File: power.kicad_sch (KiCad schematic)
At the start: 29 parts, among them J3 Conn_01x03_Male, Q1 DMP1045U-7, Q2 UMW8205A, U1 TD5830B, U2 TP4056M, U3 DW01A-G

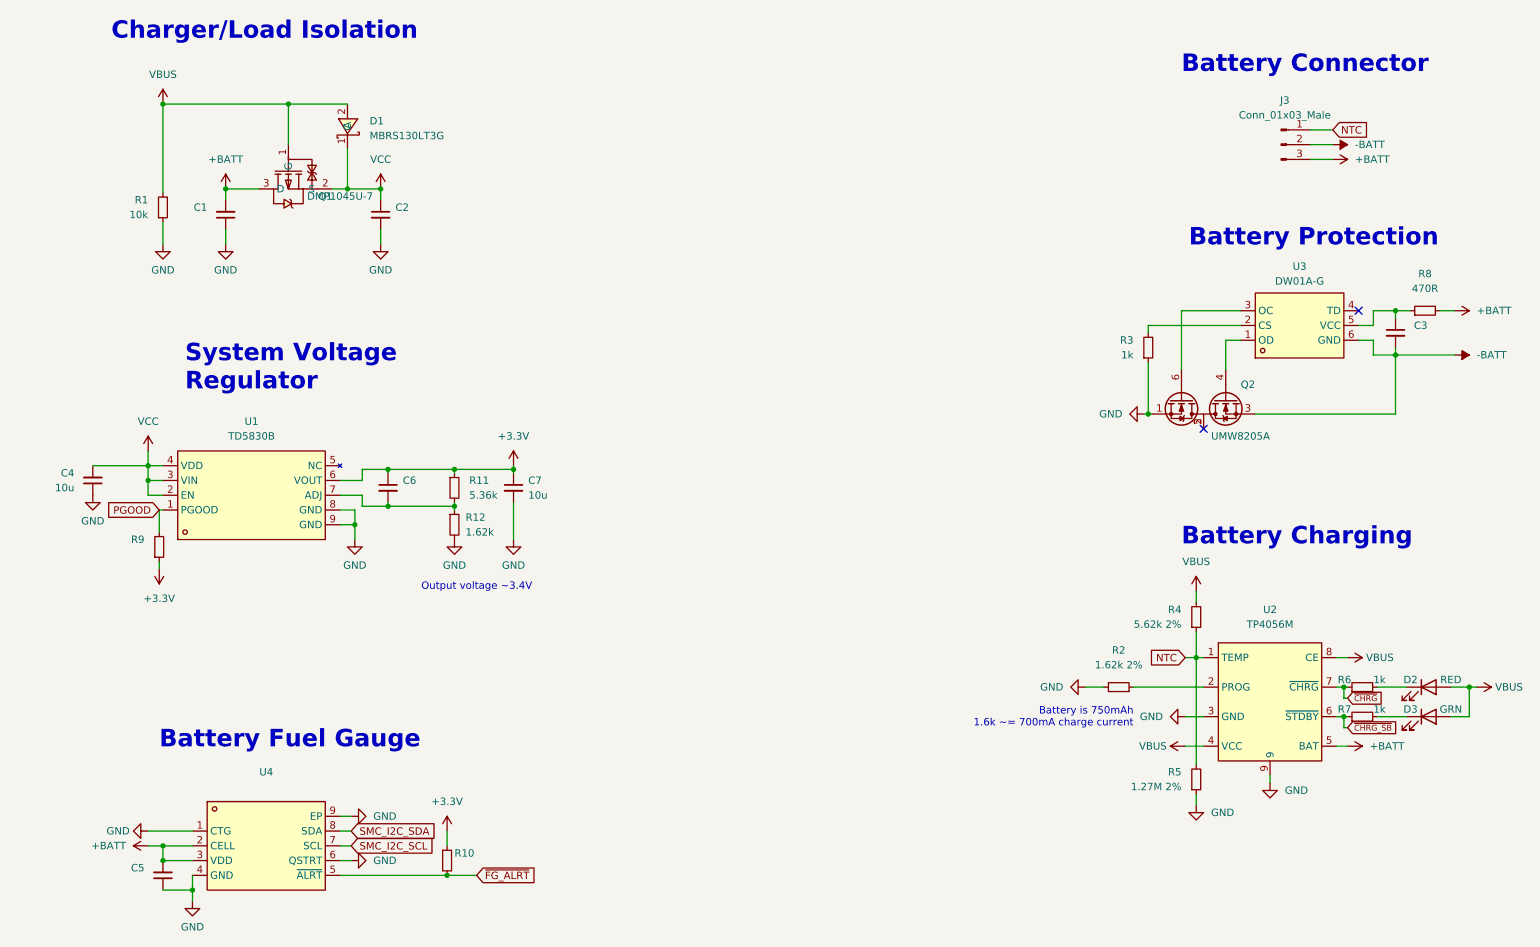
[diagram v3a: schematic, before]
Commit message: analysis: specify pi will be powered directly from VCC
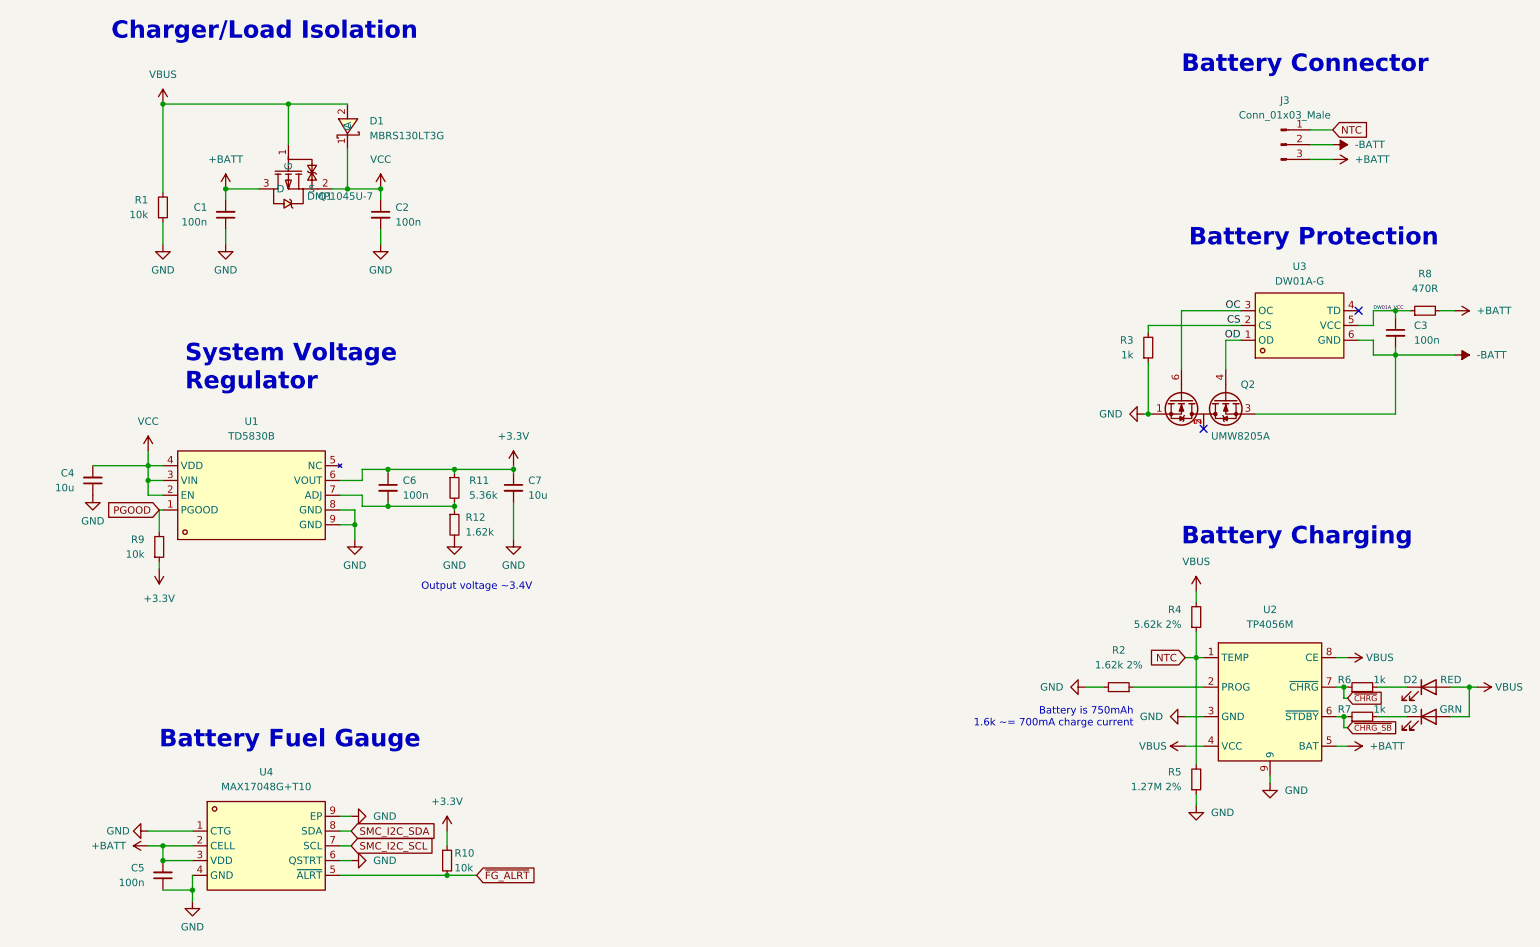
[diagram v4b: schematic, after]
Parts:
- C1, C2, C3, C5, C6: value (none) -> 100n; footprint (none) -> Capacitor_SMD:C_0402_1005Metric
- C4, C7: footprint (none) -> Capacitor_SMD:C_0402_1005Metric
- D2, D3: footprint (none) -> LED_SMD:LED_0201_0603Metric
- R1, R11, R12, R2, R3, R4, R5, R6, R7, R8: footprint (none) -> Resistor_SMD:R_0402_1005Metric
- R10, R9: value (none) -> 10k; footprint (none) -> Resistor_SMD:R_0402_1005Metric
- U4: value (none) -> MAX17048G+T10
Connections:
- net OD: now reaches Q2.4 (G2), U3.1 (OD)
- net CS: now reaches R3.2, U3.2 (CS)
- net OC: now reaches Q2.6 (G1), U3.3 (OC)
- net DW01A_VCC: now reaches C3.1, R8.1, U3.5 (VCC)
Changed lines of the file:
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@@
     (effects (font (size 3 3) (thickness 0.6) bold) (justify left bottom))
+  )
+  (label "DW01A_VCC" (at 253.365 67.945 0)
+    (effects (font (size 0.6 0.6)) (justify left bottom))
+  )
+  (label "OC" (at 230.505 67.945 180)
+    (effects (font (size 1.27 1.27)) (justify right bottom))
+  )
+  (label "CS" (at 230.505 70.485 180)
+    (effects (font (size 1.27 1.27)) (justify right bottom))
+  )
+  (label "OD" (at 230.505 73.025 180)
+    (effects (font (size 1.27 1.27)) (justify right bottom))
   )
   (global_label "PGOOD" (shape input) (at 44.45 102.235 180) (fields_autoplaced)
@@
       (effects (font (size 1.27 1.27)) (justify right))
     )
-    (property "Footprint" "" (id 2) (at 45.085 50.165 0)
+    (property "Footprint" "Resistor_SMD:R_0402_1005Metric" (id 2) (at 45.085 50.165 0)
       (effects (font (size 1.27 1.27)) hide)
     )
@@
       (effects (font (size 1.27 1.27)) (justify right))
     )
-    (property "Footprint" "" (id 2) (at 33.02 97.155 0)
+    (property "Footprint" "Capacitor_SMD:C_0402_1005Metric" (id 2) (at 33.02 97.155 0)
       (effects (font (size 1.27 1.27)) hide)
     )
@@
       (effects (font (size 1.27 1.27)) (justify right))
     )
-    (property "Footprint" "" (id 2) (at 222.885 120.65 0)
+    (property "Footprint" "Resistor_SMD:R_0402_1005Metric" (id 2) (at 222.885 120.65 0)
       (effects (font (size 1.27 1.27)) hide)
     )
@@
     )
     (property "Value" "RED" (id 1) (at 266.7 131.445 0))
-    (property "Footprint" "" (id 2) (at 262.89 132.715 0)
+    (property "Footprint" "LED_SMD:LED_0201_0603Metric" (id 2) (at 262.89 132.715 0)
       (effects (font (size 1.27 1.27)) hide)
     )
@@
       (effects (font (size 1.27 1.27)) (justify right))
     )
-    (property "Footprint" "" (id 2) (at 251.46 132.715 0)
+    (property "Footprint" "Resistor_SMD:R_0402_1005Metric" (id 2) (at 251.46 132.715 0)
       (effects (font (size 1.27 1.27)) hide)
     )
@@
     )
     (property "Value" "GRN" (id 1) (at 266.7 136.525 0))
-    (property "Footprint" "" (id 2) (at 262.89 137.795 0)
+    (property "Footprint" "LED_SMD:LED_0201_0603Metric" (id 2) (at 262.89 137.795 0)
       (effects (font (size 1.27 1.27)) hide)
     )
@@
       (effects (font (size 1.27 1.27)) (justify left))
     )
-    (property "Footprint" "" (id 2) (at 105.41 98.425 0)
+    (property "Footprint" "Capacitor_SMD:C_0402_1005Metric" (id 2) (at 105.41 98.425 0)
       (effects (font (size 1.27 1.27)) hide)
     )
@@
     (property "Reference" "R2" (id 0) (at 209.55 126.365 90))
     (property "Value" "1.62k 2%" (id 1) (at 209.55 128.905 90))
-    (property "Footprint" "" (id 2) (at 209.55 132.715 0)
+    (property "Footprint" "Resistor_SMD:R_0402_1005Metric" (id 2) (at 209.55 132.715 0)
       (effects (font (size 1.27 1.27)) hide)
     )
@@
       (effects (font (size 1.27 1.27)) (justify right))
     )
-    (property "Footprint" "" (id 2) (at 251.46 137.795 0)
+    (property "Footprint" "Resistor_SMD:R_0402_1005Metric" (id 2) (at 251.46 137.795 0)
       (effects (font (size 1.27 1.27)) hide)
     )
@@
       (effects (font (size 1.27 1.27)) (justify left))
     )
-    (property "Value" "" (id 1) (at 260.35 73.0312 0)
-      (effects (font (size 1.27 1.27)) (justify left))
-    )
-    (property "Footprint" "" (id 2) (at 257.175 71.755 0)
+    (property "Value" "100n" (id 1) (at 260.35 73.0312 0)
+      (effects (font (size 1.27 1.27)) (justify left))
+    )
+    (property "Footprint" "Capacitor_SMD:C_0402_1005Metric" (id 2) (at 257.175 71.755 0)
       (effects (font (size 1.27 1.27)) hide)
     )
@@
     (property "Reference" "R8" (id 0) (at 262.255 61.595 90))
     (property "Value" "470R" (id 1) (at 262.255 64.135 90))
-    (property "Footprint" "" (id 2) (at 262.255 67.945 0)
+    (property "Footprint" "Resistor_SMD:R_0402_1005Metric" (id 2) (at 262.255 67.945 0)
       (effects (font (size 1.27 1.27)) hide)
     )
@@
       (effects (font (size 1.27 1.27)) (justify right))
     )
-    (property "Value" "" (id 1) (at 41.91 109.8549 0)
-      (effects (font (size 1.27 1.27)) (justify right))
-    )
-    (property "Footprint" "" (id 2) (at 44.45 108.585 0)
+    (property "Value" "10k" (id 1) (at 41.91 109.8549 0)
+      (effects (font (size 1.27 1.27)) (justify right))
+    )
+    (property "Footprint" "Resistor_SMD:R_0402_1005Metric" (id 2) (at 44.45 108.585 0)
       (effects (font (size 1.27 1.27)) hide)
     )
@@
       (effects (font (size 1.27 1.27)) (justify right))
     )
-    (property "Value" "" (id 1) (at 52.705 52.6985 0)
-      (effects (font (size 1.27 1.27)) (justify right))
-    )
-    (property "Footprint" "" (id 2) (at 55.88 51.435 0)
+    (property "Value" "100n" (id 1) (at 52.705 52.6985 0)
+      (effects (font (size 1.27 1.27)) (justify right))
+    )
+    (property "Footprint" "Capacitor_SMD:C_0402_1005Metric" (id 2) (at 55.88 51.435 0)
       (effects (font (size 1.27 1.27)) hide)
     )
@@
       (effects (font (size 1.27 1.27)) (justify left))
     )
-    (property "Value" "" (id 1) (at 95.25 163.83 0)
-      (effects (font (size 1.27 1.27)) (justify left))
-    )
-    (property "Footprint" "" (id 2) (at 93.98 162.56 0)
+    (property "Value" "10k" (id 1) (at 95.25 163.83 0)
+      (effects (font (size 1.27 1.27)) (justify left))
+    )
+    (property "Footprint" "Resistor_SMD:R_0402_1005Metric" (id 2) (at 93.98 162.56 0)
       (effects (font (size 1.27 1.27)) hide)
     )
@@
       (effects (font (size 1.27 1.27)) (justify left))
     )
-    (property "Footprint" "" (id 2) (at 95.25 98.425 0)
+    (property "Footprint" "Resistor_SMD:R_0402_1005Metric" (id 2) (at 95.25 98.425 0)
       (effects (font (size 1.27 1.27)) hide)
     )
@@
       (effects (font (size 1.27 1.27)) (justify left))
     )
-    (property "Value" "" (id 1) (at 86.36 99.7012 0)
-      (effects (font (size 1.27 1.27)) (justify left))
-    )
-    (property "Footprint" "" (id 2) (at 83.82 98.425 0)
+    (property "Value" "100n" (id 1) (at 86.36 99.7012 0)
+      (effects (font (size 1.27 1.27)) (justify left))
+    )
+    (property "Footprint" "Capacitor_SMD:C_0402_1005Metric" (id 2) (at 83.82 98.425 0)
       (effects (font (size 1.27 1.27)) hide)
     )
@@
       (effects (font (size 1.27 1.27)) (justify left))
     )
-    (property "Footprint" "" (id 2) (at 95.25 104.775 0)
+    (property "Footprint" "Resistor_SMD:R_0402_1005Metric" (id 2) (at 95.25 104.775 0)
       (effects (font (size 1.27 1.27)) hide)
     )
@@
       (effects (font (size 1.27 1.27)) (justify left))
     )
-    (property "Value" "" (id 1) (at 85.09 52.7112 0)
-      (effects (font (size 1.27 1.27)) (justify left))
-    )
-    (property "Footprint" "" (id 2) (at 82.55 51.435 0)
+    (property "Value" "100n" (id 1) (at 85.09 52.7112 0)
+      (effects (font (size 1.27 1.27)) (justify left))
+    )
+    (property "Footprint" "Capacitor_SMD:C_0402_1005Metric" (id 2) (at 82.55 51.435 0)
       (effects (font (size 1.27 1.27)) hide)
     )
@@
       (effects (font (size 1.27 1.27)) (justify right))
     )
-    (property "Footprint" "" (id 2) (at 214.63 74.295 0)
+    (property "Footprint" "Resistor_SMD:R_0402_1005Metric" (id 2) (at 214.63 74.295 0)
       (effects (font (size 1.27 1.27)) hide)
     )
@@
       (effects (font (size 1.27 1.27)) (justify right))
     )
-    (property "Footprint" "" (id 2) (at 222.885 148.59 0)
+    (property "Footprint" "Resistor_SMD:R_0402_1005Metric" (id 2) (at 222.885 148.59 0)
       (effects (font (size 1.27 1.27)) hide)
     )
@@
       (effects (font (size 1.27 1.27)) (justify right))
     )
-    (property "Value" "" (id 1) (at 41.91 166.3635 0)
-      (effects (font (size 1.27 1.27)) (justify right))
-    )
-    (property "Footprint" "" (id 2) (at 45.085 165.1 0)
+    (property "Value" "100n" (id 1) (at 41.91 166.3635 0)
+      (effects (font (size 1.27 1.27)) (justify right))
+    )
+    (property "Footprint" "Capacitor_SMD:C_0402_1005Metric" (id 2) (at 45.085 165.1 0)
       (effects (font (size 1.27 1.27)) hide)
     )
@@
     (in_bom yes) (on_board yes) (fields_autoplaced)
     (property "Reference" "U4" (id 0) (at 62.865 147.32 0))
-    (property "Value" "" (id 1) (at 62.865 149.86 0))
+    (property "Value" "MAX17048G+T10" (id 1) (at 62.865 149.86 0))
     (property "Footprint" "lcsc:DFN-8_L2.0-W2.0-P0.50-BL-EP" (id 2) (at 62.865 172.72 0)
       (effects (font (size 1.27 1.27)) hide)

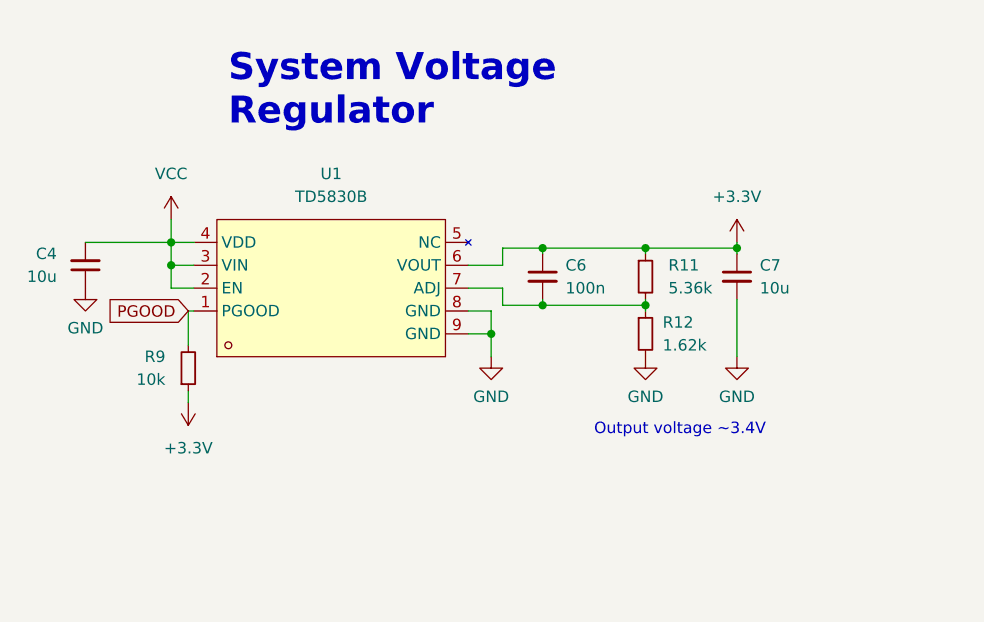
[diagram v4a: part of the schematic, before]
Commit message: analysis: change system regulator to one with lower dropout
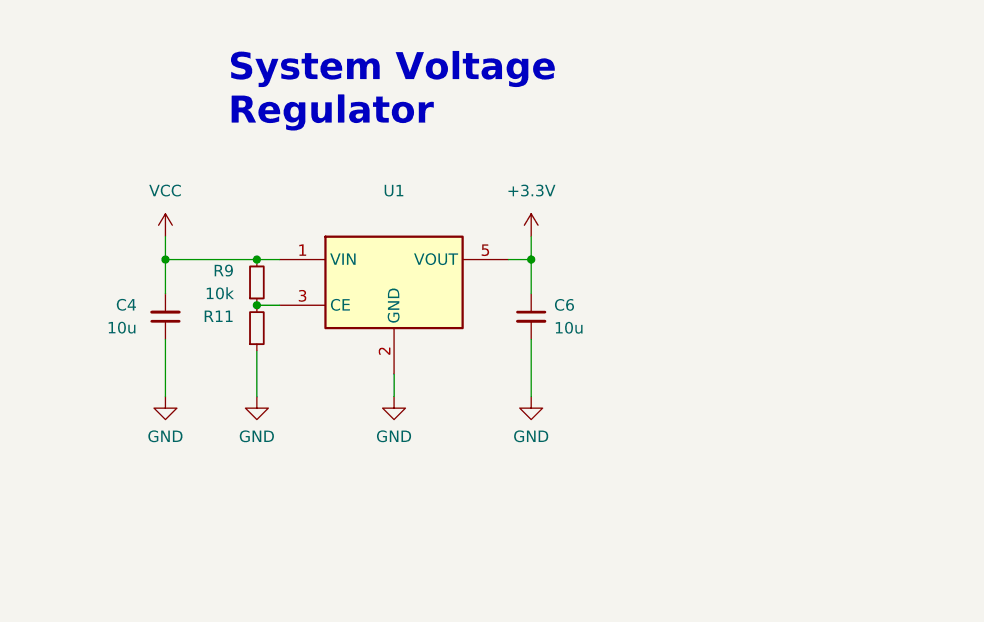
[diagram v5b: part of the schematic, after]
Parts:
- removed C7: 10u, Capacitor_SMD:C_0402_1005Metric, symbol Device:C_Small
- removed R12: 1.62k, Resistor_SMD:R_0402_1005Metric, symbol Device:R_Small
- removed U1: TD5830B, lcsc:SOP-8_L4.9-W3.9-P1.27-LS6.0-BL-EP, symbol lcsc:TD5830B
- added U1: (no value), symbol Regulator_Linear:XC6210B332MR
- C6: value 100n -> 10u
- R11: value 5.36k -> (none)
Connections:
- net PGOOD is gone; now on net VCC: R9.2
- net +3V3: now also U1.5 (VOUT); no longer R11.1, R9.1
- net GND: now also C6.2, R11.1, U1.2 (GND)
- net VCC: now also U1.1 (VIN)
- net at R11.2: now also R9.1, U1.3 (CE); no longer C6.2
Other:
- note removed: "Output voltage ~3.4V"

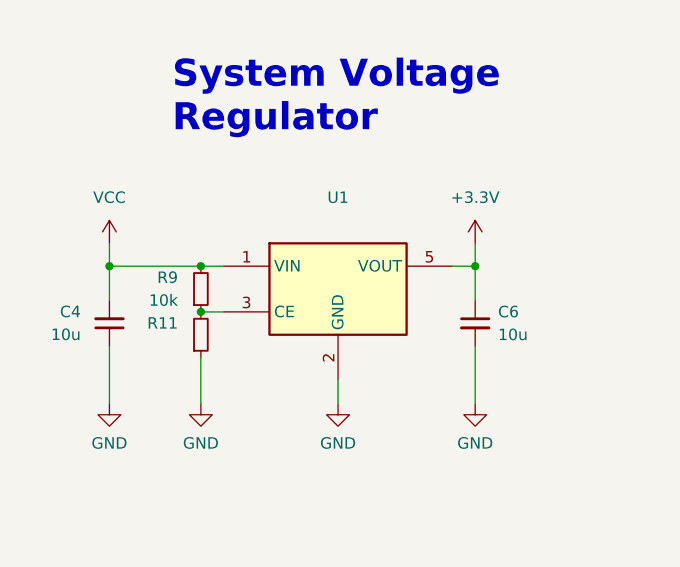
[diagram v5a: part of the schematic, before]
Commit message: schem: add MOSFET to drive clickwheel
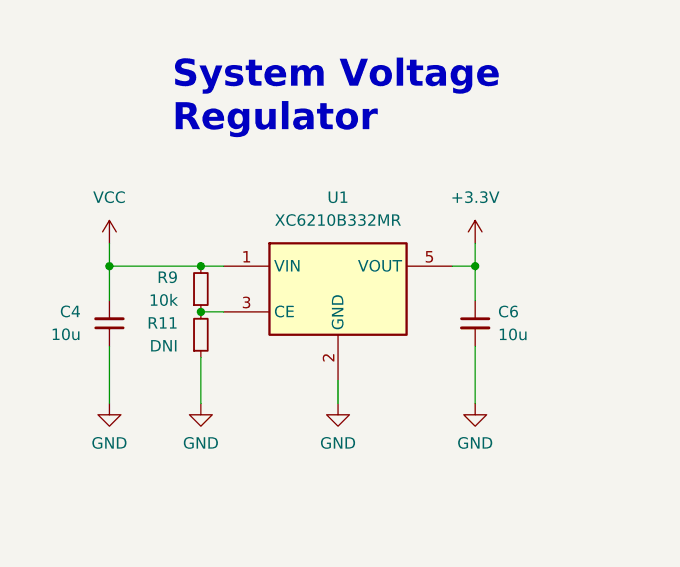
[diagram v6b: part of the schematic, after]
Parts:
- R11: value (none) -> DNI
- U1: value (none) -> XC6210B332MR; footprint (none) -> Package_TO_SOT_SMD:SOT-23-5
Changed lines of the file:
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@@
     (in_bom yes) (on_board yes) (fields_autoplaced)
     (property "Reference" "U1" (id 0) (at 67.31 88.9 0))
-    (property "Value" "" (id 1) (at 67.31 91.44 0))
-    (property "Footprint" "" (id 2) (at 67.31 99.06 0)
+    (property "Value" "XC6210B332MR" (id 1) (at 67.31 91.44 0))
+    (property "Footprint" "Package_TO_SOT_SMD:SOT-23-5" (id 2) (at 67.31 99.06 0)
       (effects (font (size 1.27 1.27)) hide)
     )
@@
       (effects (font (size 1.27 1.27)) (justify right))
     )
-    (property "Value" "" (id 1) (at 49.53 105.4099 0)
-      (effects (font (size 1.27 1.27)) (justify right))
-    )
+    (property "Value" "DNI" (id 1) (at 49.53 105.4099 0)
+      (effects (font (size 1.27 1.27)) (justify right))
+    )
